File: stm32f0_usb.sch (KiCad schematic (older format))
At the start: 32 parts, among them J1 USB_B_Mini, J2 Conn_ARM_JTAG_SWD_10, J3 Conn_01x14_Male, J4 Conn_01x14_Male, SW1 B3S-1000P, SW2 B3S-1000P, U2 ADP121-AUJZ33R7, U3 USBLC6-2SC6

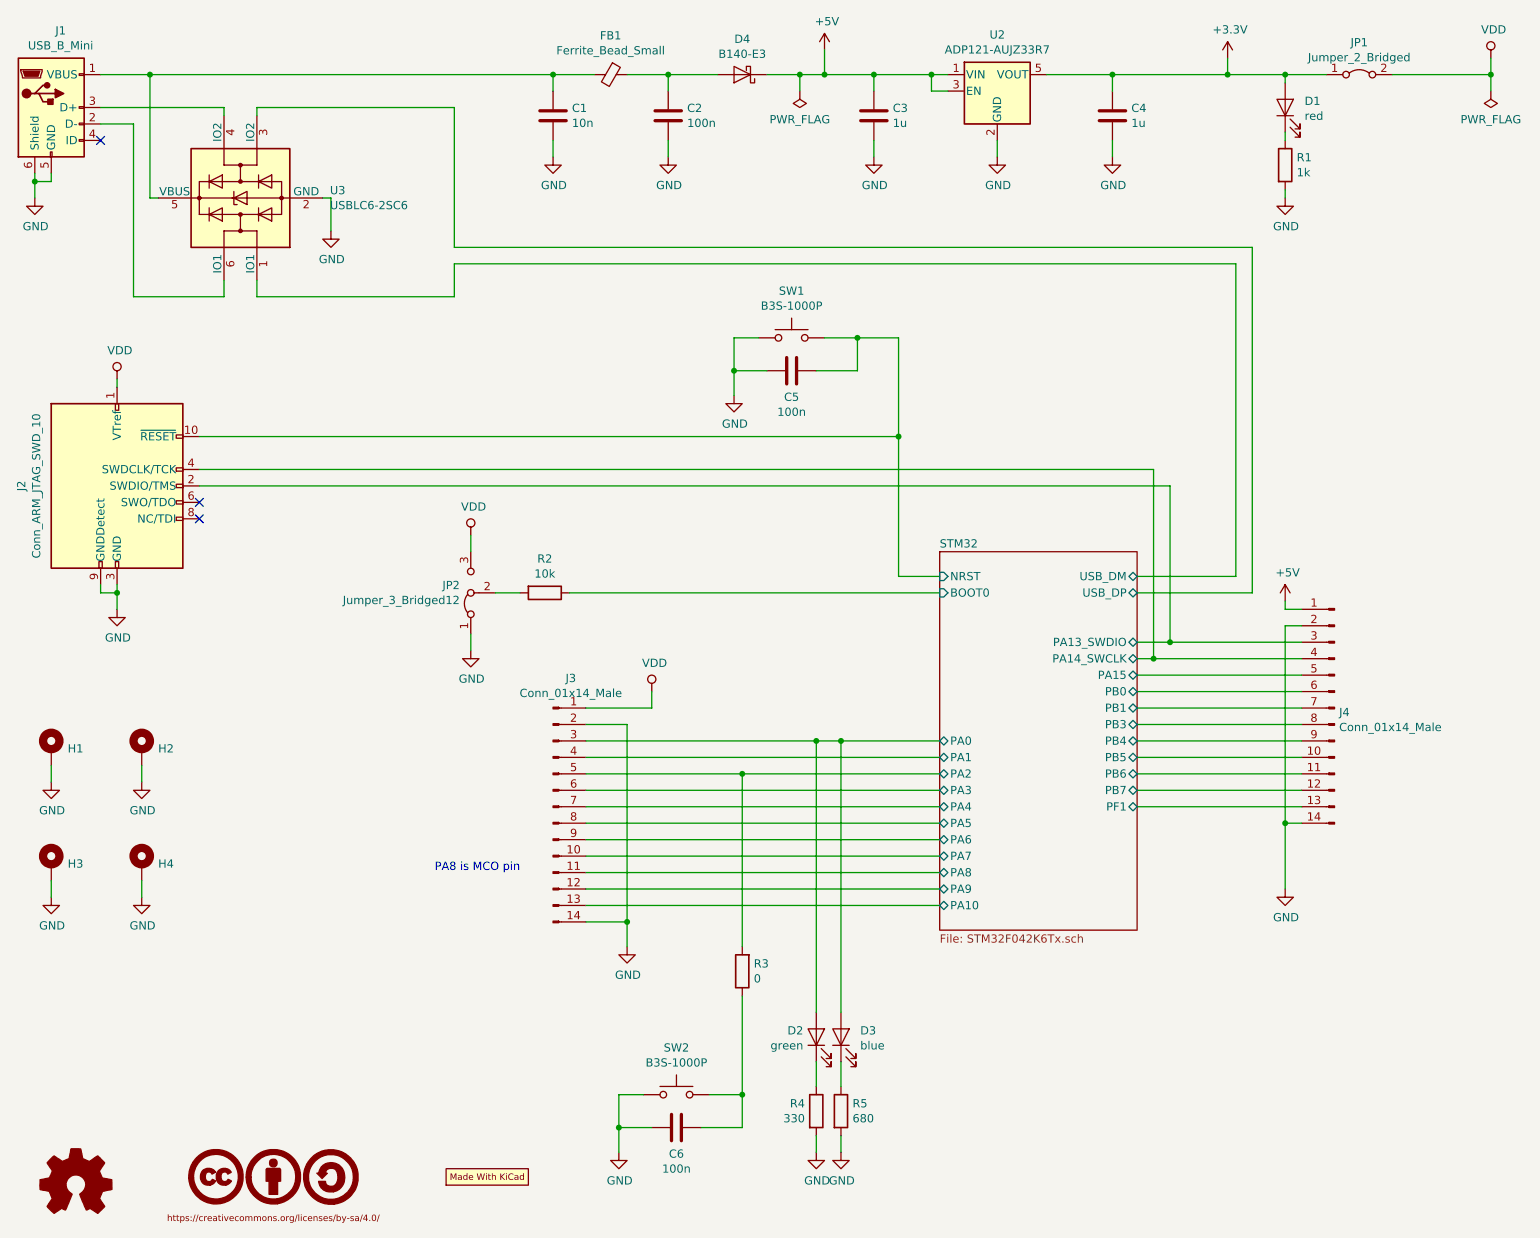
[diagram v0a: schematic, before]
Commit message: update GPIO/header pinout to ease routing
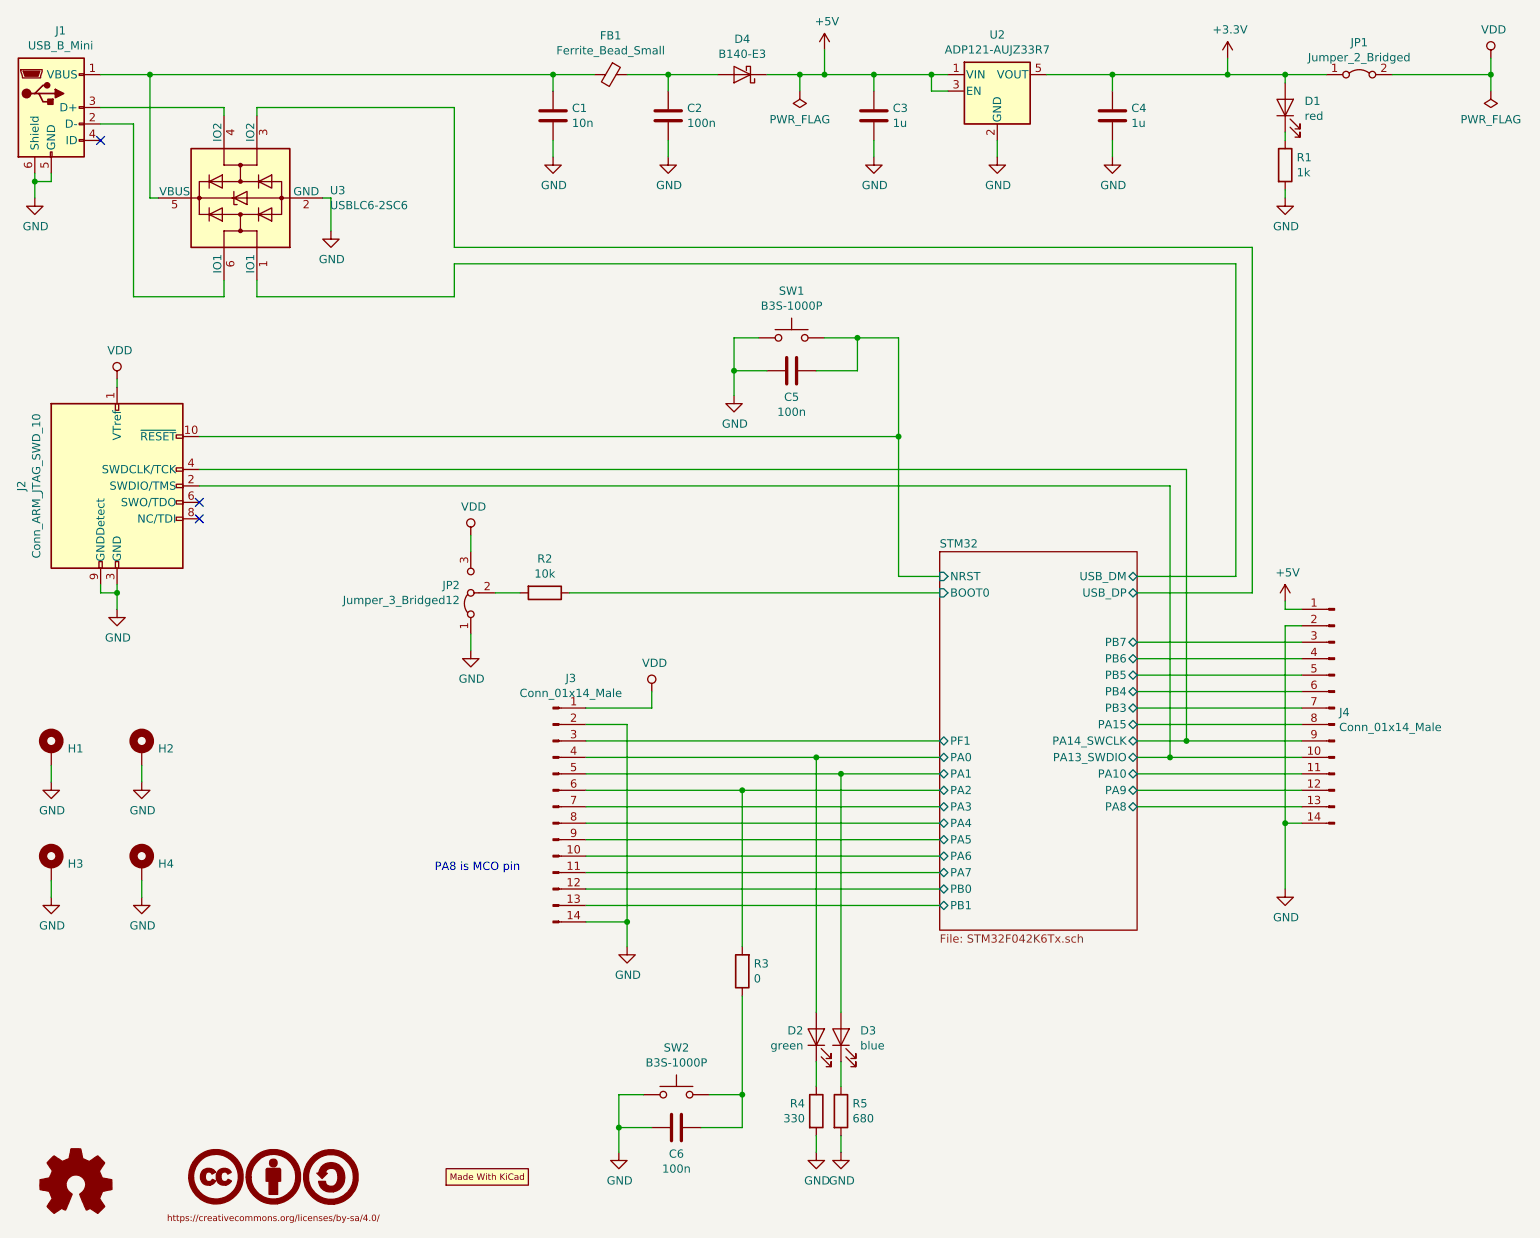
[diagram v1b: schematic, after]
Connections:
- net STM32/PA0: now also J3.4 (Pin_4); no longer D3.2 (A), J3.3 (Pin_3)
- net STM32/PA1: now also D3.2 (A), J3.5 (Pin_5); no longer J3.4 (Pin_4)
- net STM32/PA10: now also J4.11 (Pin_11); no longer J3.13 (Pin_13)
- net STM32/PA13_SWDIO: now also J4.10 (Pin_10); no longer J4.3 (Pin_3)
- net STM32/PA14_SWCLK: now also J4.9 (Pin_9); no longer J4.4 (Pin_4)
- net STM32/PA15: now also J4.8 (Pin_8); no longer J4.5 (Pin_5)
- net STM32/PA2: now also J3.6 (Pin_6); no longer J3.5 (Pin_5)
- net STM32/PA3: now also J3.7 (Pin_7); no longer J3.6 (Pin_6)
- net STM32/PA4: now also J3.8 (Pin_8); no longer J3.7 (Pin_7)
- net STM32/PA5: now also J3.9 (Pin_9); no longer J3.8 (Pin_8)
- net STM32/PA6: now also J3.10 (Pin_10); no longer J3.9 (Pin_9)
- net STM32/PA7: now also J3.11 (Pin_11); no longer J3.10 (Pin_10)
- net STM32/PA8: now also J4.13 (Pin_13); no longer J3.11 (Pin_11)
- net STM32/PA9: now also J4.12 (Pin_12); no longer J3.12 (Pin_12)
- net STM32/PB0: now also J3.12 (Pin_12); no longer J4.6 (Pin_6)
- net STM32/PB1: now also J3.13 (Pin_13); no longer J4.7 (Pin_7)
- net STM32/PB3: now also J4.7 (Pin_7); no longer J4.8 (Pin_8)
- net STM32/PB4: now also J4.6 (Pin_6); no longer J4.9 (Pin_9)
- net STM32/PB5: now also J4.5 (Pin_5); no longer J4.10 (Pin_10)
- net STM32/PB6: now also J4.4 (Pin_4); no longer J4.11 (Pin_11)
- net STM32/PB7: now also J4.3 (Pin_3); no longer J4.12 (Pin_12)
- net STM32/PF1: now also J3.3 (Pin_3); no longer J4.13 (Pin_13)
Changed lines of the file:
@@
 $EndComp
 Wire Wire Line
-	4150 5300 6300 5300
+	4150 5300 5100 5300
 Wire Wire Line
 	6300 5400 4150 5400
@@
 	6300 6000 4150 6000
 Wire Wire Line
-	4150 5200 5100 5200
-Wire Wire Line
-	4150 5000 5550 5000
-Wire Wire Line
-	4150 5100 6300 5100
-Wire Wire Line
-	5550 6650 5550 5000
-Connection ~ 5550 5000
-Wire Wire Line
-	5550 5000 5700 5000
-Wire Wire Line
-	5700 5000 5700 6650
-Connection ~ 5700 5000
-Wire Wire Line
-	5700 5000 6300 5000
-Wire Wire Line
-	5100 6250 5100 5200
-Connection ~ 5100 5200
-Wire Wire Line
-	5100 5200 6300 5200
+	4150 5100 5550 5100
 Text Notes 3750 5800 2    50   ~ 0
 PA8 is MCO pin
@@
 F1 "STM32F042K6Tx.sch" 50
 F2 "BOOT0" I L 6300 4100 50
-F3 "PF1" B R 7500 5400 50
-F4 "PB0" B R 7500 4700 50
-F5 "PB1" B R 7500 4800 50
-F6 "PB3" B R 7500 4900 50
-F7 "PB4" B R 7500 5000 50
-F8 "PB5" B R 7500 5100 50
-F9 "PB6" B R 7500 5200 50
-F10 "PB7" B R 7500 5300 50
+F3 "PF1" B L 6300 5000 50
+F4 "PB0" B L 6300 5900 50
+F5 "PB1" B L 6300 6000 50
+F6 "PB3" B R 7500 4800 50
+F7 "PB4" B R 7500 4700 50
+F8 "PB5" B R 7500 4600 50
+F9 "PB6" B R 7500 4500 50
+F10 "PB7" B R 7500 4400 50
 F11 "USB_DM" B R 7500 4000 50
 F12 "USB_DP" B R 7500 4100 50
-F13 "PA15" B R 7500 4600 50
-F14 "PA10" B L 6300 6000 50
-F15 "PA9" B L 6300 5900 50
-F16 "PA0" B L 6300 5000 50
-F17 "PA1" B L 6300 5100 50
-F18 "PA2" B L 6300 5200 50
-F19 "PA3" B L 6300 5300 50
-F20 "PA4" B L 6300 5400 50
-F21 "PA5" B L 6300 5500 50
-F22 "PA6" B L 6300 5600 50
-F23 "PA7" B L 6300 5700 50
-F24 "PA8" B L 6300 5800 50
+F13 "PA15" B R 7500 4900 50
+F14 "PA10" B R 7500 5200 50
+F15 "PA9" B R 7500 5300 50
+F16 "PA0" B L 6300 5100 50
+F17 "PA1" B L 6300 5200 50
+F18 "PA2" B L 6300 5300 50
+F19 "PA3" B L 6300 5400 50
+F20 "PA4" B L 6300 5500 50
+F21 "PA5" B L 6300 5600 50
+F22 "PA6" B L 6300 5700 50
+F23 "PA7" B L 6300 5800 50
+F24 "PA8" B R 7500 5400 50
 F25 "NRST" I L 6300 4000 50
-F26 "PA13_SWDIO" B R 7500 4400 50
-F27 "PA14_SWCLK" B R 7500 4500 50
+F26 "PA13_SWDIO" B R 7500 5100 50
+F27 "PA14_SWCLK" B R 7500 5000 50
 $EndSheet
 Connection ~ 800  1600
@@
 Wire Wire Line
 	6050 4000 6300 4000
-Wire Wire Line
-	7500 4500 7600 4500
-Wire Wire Line
-	7500 4400 7700 4400
 $Comp
 L Device:Ferrite_Bead_Small FB1
@@
 	4400 950  4650 950
 Wire Wire Line
-	7700 4400 8500 4400
-Connection ~ 7700 4400
-Wire Wire Line
-	7600 4500 8500 4500
-Connection ~ 7600 4500
-Wire Wire Line
-	7500 4600 8500 4600
-Wire Wire Line
-	7500 4700 8500 4700
-Wire Wire Line
-	7500 4800 8500 4800
-Wire Wire Line
-	7500 4900 8500 4900
-Wire Wire Line
-	7500 5000 8500 5000
-Wire Wire Line
-	7500 5100 8500 5100
-Wire Wire Line
-	7500 5200 8500 5200
-Wire Wire Line
-	7500 5300 8500 5300
-Wire Wire Line
-	7500 5400 8500 5400
-Wire Wire Line
 	7500 4000 8100 4000
 Wire Wire Line
@@
 	1300 4100 1300 4050
 Wire Wire Line
-	7700 3450 7700 4400
-Wire Wire Line
-	7600 3350 7600 4500
-Wire Wire Line
 	6050 3150 6050 4000
 Wire Wire Line
 	1800 3450 7700 3450
 Wire Wire Line
-	1800 3350 7600 3350
+	1800 3350 7800 3350
 Wire Wire Line
 	1800 3150 6050 3150
@@
 Wire Wire Line
 	5450 950  5250 950
+Wire Wire Line
+	7800 5000 7500 5000
+Wire Wire Line
+	7800 3350 7800 5000
+Wire Wire Line
+	7500 5100 7700 5100
+Wire Wire Line
+	7700 3450 7700 5100
+Wire Wire Line
+	7800 5000 8500 5000
+Connection ~ 7800 5000
+Connection ~ 7700 5100
+Wire Wire Line
+	4150 5200 5700 5200
+Wire Wire Line
+	5100 6250 5100 5300
+Connection ~ 5100 5300
+Wire Wire Line
+	5100 5300 6300 5300
+Wire Wire Line
+	4150 5000 6300 5000
+Wire Wire Line
+	5550 6650 5550 5100
+Connection ~ 5550 5100
+Wire Wire Line
+	5550 5100 6300 5100
+Wire Wire Line
+	5700 6650 5700 5200
+Connection ~ 5700 5200
+Wire Wire Line
+	5700 5200 6300 5200
+Wire Wire Line
+	7500 4400 8500 4400
+Wire Wire Line
+	8500 4500 7500 4500
+Wire Wire Line
+	8500 4600 7500 4600
+Wire Wire Line
+	8500 4700 7500 4700
+Wire Wire Line
+	8500 4800 7500 4800
+Wire Wire Line
+	8500 5100 7700 5100
+Wire Wire Line
+	8500 4900 7500 4900
+Wire Wire Line
+	8500 5200 7500 5200
+Wire Wire Line
+	8500 5300 7500 5300
+Wire Wire Line
+	8500 5400 7500 5400
 $EndSCHEMATC

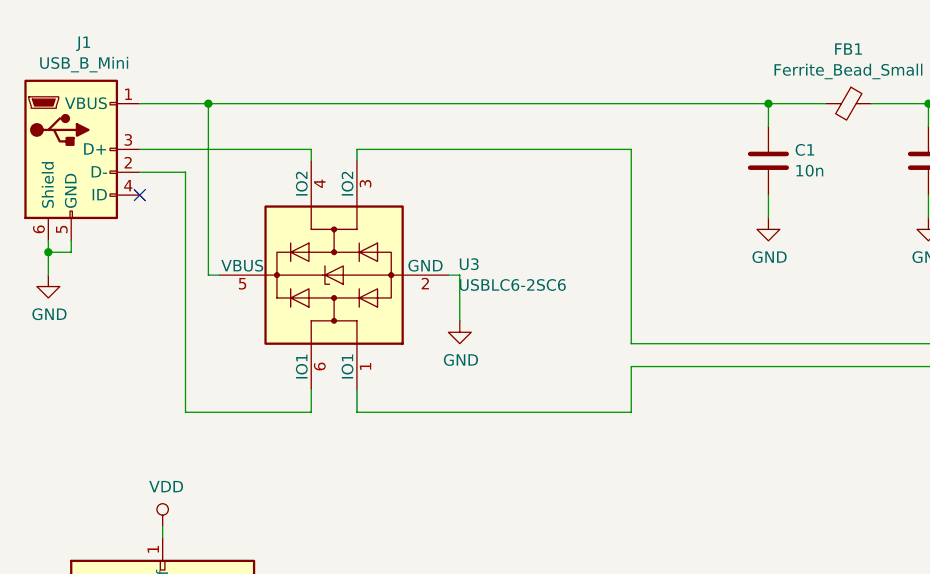
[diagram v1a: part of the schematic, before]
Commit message: update usb esd connections
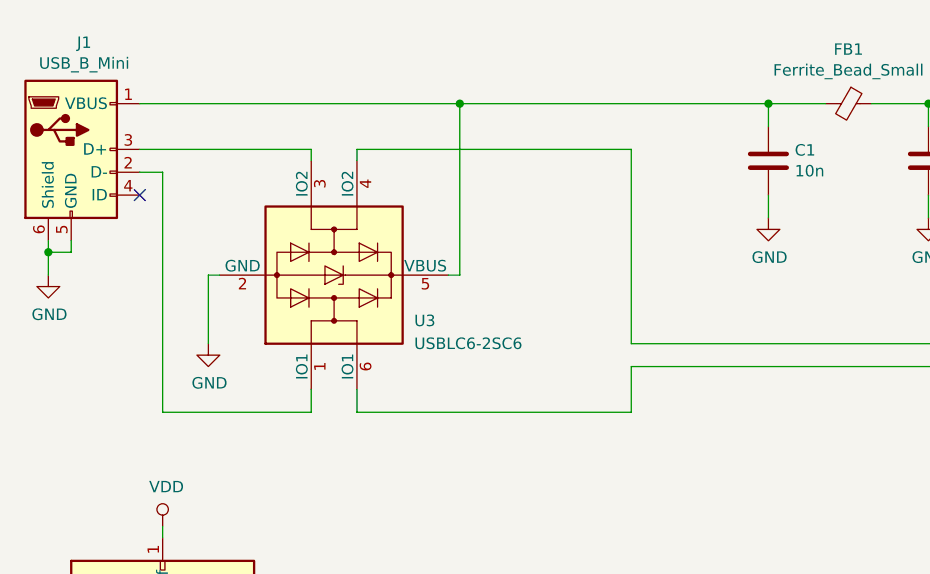
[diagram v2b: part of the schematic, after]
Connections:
- net STM32/USB_DM: now also U3.6 (IO1); no longer U3.1 (IO1)
- net STM32/USB_DP: now also U3.4 (IO2); no longer U3.3 (IO2)
- net at J1.3 (D+): now also U3.3 (IO2); no longer U3.4 (IO2)
- net at J1.2 (D-): now also U3.1 (IO1); no longer U3.6 (IO1)
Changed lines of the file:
@@
 U 1 1 5E184338
 P 2050 1700
-F 0 "U3" V 2096 1156 50  0000 R CNN
-F 1 "USBLC6-2SC6" V 2005 1156 50  0000 R CNN
+F 0 "U3" V 1850 2050 50  0000 L CNN
+F 1 "USBLC6-2SC6" V 1750 2050 50  0000 L CNN
 F 2 "Package_TO_SOT_SMD:SOT-23-6" H 1300 2100 50  0001 C CNN
 F 3 "http://www2.st.com/resource/en/datasheet/CD00050750.pdf" H 2250 2050 50  0001 C CNN
 	1    2050 1700
-	0    -1   -1   0
+	0    1    -1   0
 $EndComp
 $Comp
 L power:GND #PWR08
 U 1 1 5E195B29
-P 2600 1900
-F 0 "#PWR08" H 2600 1650 50  0001 C CNN
-F 1 "GND" H 2605 1727 50  0000 C CNN
-F 2 "" H 2600 1900 50  0001 C CNN
-F 3 "" H 2600 1900 50  0001 C CNN
-	1    2600 1900
+P 1500 2000
+F 0 "#PWR08" H 1500 1750 50  0001 C CNN
+F 1 "GND" H 1505 1827 50  0000 C CNN
+F 2 "" H 1500 2000 50  0001 C CNN
+F 3 "" H 1500 2000 50  0001 C CNN
+	1    1500 2000
 	1    0    0    -1
 $EndComp
@@
 Connection ~ 5600 950
 Wire Wire Line
-	1200 950  1500 950
-Wire Wire Line
 	1950 1150 1950 1200
 Wire Wire Line
@@
 	8200 2000 8200 4100
 Wire Wire Line
-	1400 1250 1400 2300
-Wire Wire Line
-	1400 2300 1950 2300
+	1300 1250 1300 2300
+Wire Wire Line
+	1300 2300 1950 2300
 Wire Wire Line
 	1950 2300 1950 2200
 Wire Wire Line
-	1200 1250 1400 1250
+	1200 1250 1300 1250
 Wire Wire Line
 	2150 2200 2150 2300
@@
 	3350 2100 8100 2100
 Wire Wire Line
-	2600 1900 2600 1700
-Wire Wire Line
-	2600 1700 2550 1700
-Wire Wire Line
 	1550 1700 1500 1700
-Wire Wire Line
-	1500 1700 1500 950
 $Comp
 L Device:C C2
@@
 Wire Wire Line
 	3950 1450 3950 1350
-Wire Wire Line
-	1500 950  3950 950
-Connection ~ 1500 950
 Wire Wire Line
 	4650 950  4950 950
@@
 Wire Wire Line
 	8500 5400 7500 5400
+Wire Wire Line
+	1200 950  2600 950
+Wire Wire Line
+	1500 2000 1500 1700
+Wire Wire Line
+	2550 1700 2600 1700
+Wire Wire Line
+	2600 1700 2600 950
+Connection ~ 2600 950
+Wire Wire Line
+	2600 950  3950 950
 $EndSCHEMATC

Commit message: initial routing mostly finished
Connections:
- net VBUS: now reaches C1.1, FB1.2, J1.1 (VBUS), U3.5 (VBUS)
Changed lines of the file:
@@
 	8500 5400 7500 5400
 Wire Wire Line
-	1200 950  2600 950
+	1200 950  1400 950
 Wire Wire Line
 	1500 2000 1500 1700
@@
 Wire Wire Line
 	2600 950  3950 950
+$Comp
+L power:VBUS #PWR0101
+U 1 1 5E298E74
+P 1400 800
+F 0 "#PWR0101" H 1400 650 50  0001 C CNN
+F 1 "VBUS" H 1415 973 50  0000 C CNN
+F 2 "" H 1400 800 50  0001 C CNN
+F 3 "" H 1400 800 50  0001 C CNN
+	1    1400 800
+	1    0    0    -1
+$EndComp
+Wire Wire Line
+	1400 800  1400 950
+Connection ~ 1400 950
+Wire Wire Line
+	1400 950  2600 950
 $EndSCHEMATC
